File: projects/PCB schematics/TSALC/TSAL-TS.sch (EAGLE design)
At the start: 29 parts, among them J1 2P_1-770166-0, J2 2P_1-770166-0, J3 2P_1-770166-0, J4 2P_1-770166-0, X2 5566-2, X3 5566-2

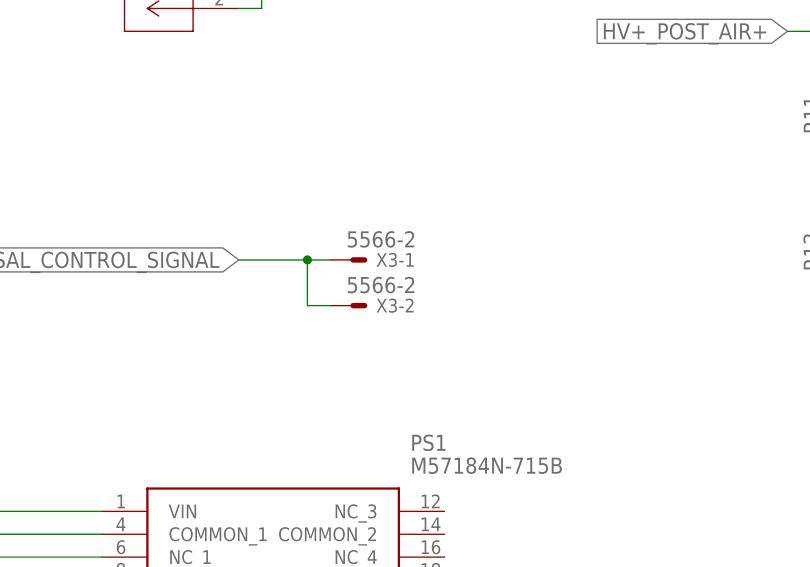
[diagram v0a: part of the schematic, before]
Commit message: TSALC - TS; Rev A.
Adding in silkscreen markings.
Board has TS and GLV markings separated by 8.26mm. This is the limit imposed by the optocoupler. The rules state that optocouplers are exempt. However, they will likely consider any copper leading up to the device to be TS components to be dealt with.

TSALC - TS; Rev A. Pull request #5.

TSALC boards now ready for pull request review.
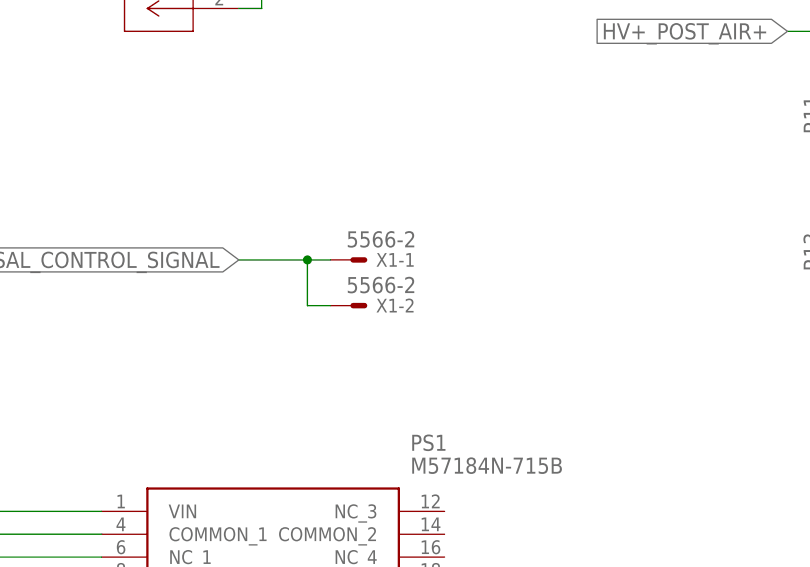
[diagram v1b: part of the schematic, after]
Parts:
- renumbered X3 to X1
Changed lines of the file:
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@@
 <part name="R2" library="rcl" library_urn="urn:adsk.eagle:library:334" deviceset="R-US_" device="R0805" package3d_urn="urn:adsk.eagle:package:23553/2" value="180"/>
 <part name="X2" library="con-molex" library_urn="urn:adsk.eagle:library:165" deviceset="5566-2" device="" package3d_urn="urn:adsk.eagle:package:8078583/1"/>
-<part name="X3" library="con-molex" library_urn="urn:adsk.eagle:library:165" deviceset="5566-2" device="" package3d_urn="urn:adsk.eagle:package:8078583/1"/>
+<part name="X1" library="con-molex" library_urn="urn:adsk.eagle:library:165" deviceset="5566-2" device="" package3d_urn="urn:adsk.eagle:package:8078583/1"/>
 <part name="PS1" library="M57184N-715B" deviceset="M57184N-715B" device=""/>
 <part name="L1" library="rcl" library_urn="urn:adsk.eagle:library:334" deviceset="L-US" device="L2012C" package3d_urn="urn:adsk.eagle:package:23475/2" value="1mH"/>
@@
 <attribute name="VALUE" x="22.098" y="75.057" size="1.778" layer="96"/>
 </instance>
-<instance part="X3" gate="-1" x="78.74" y="78.74" smashed="yes">
+<instance part="X1" gate="-1" x="78.74" y="78.74" smashed="yes">
 <attribute name="NAME" x="81.28" y="77.978" size="1.524" layer="95"/>
 <attribute name="VALUE" x="77.978" y="80.137" size="1.778" layer="96"/>
 </instance>
-<instance part="X3" gate="-2" x="78.74" y="73.66" smashed="yes">
+<instance part="X1" gate="-2" x="78.74" y="73.66" smashed="yes">
 <attribute name="NAME" x="81.28" y="72.898" size="1.524" layer="95"/>
 <attribute name="VALUE" x="77.978" y="75.057" size="1.778" layer="96"/>
@@
 <net name="TSAL_CONTROL_SIGNAL" class="0">
 <segment>
-<pinref part="X3" gate="-1" pin="S"/>
+<pinref part="X1" gate="-1" pin="S"/>
 <wire x1="76.2" y1="78.74" x2="73.66" y2="78.74" width="0.1524" layer="91"/>
 <wire x1="73.66" y1="78.74" x2="73.66" y2="73.66" width="0.1524" layer="91"/>
-<pinref part="X3" gate="-2" pin="S"/>
+<pinref part="X1" gate="-2" pin="S"/>
 <wire x1="73.66" y1="73.66" x2="76.2" y2="73.66" width="0.1524" layer="91"/>
 <wire x1="73.66" y1="78.74" x2="66.04" y2="78.74" width="0.1524" layer="91"/>

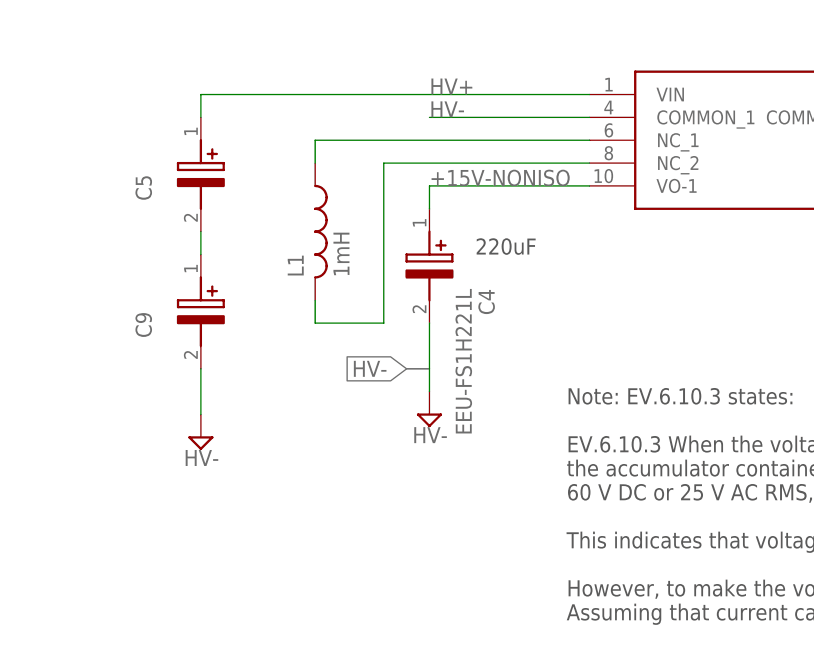
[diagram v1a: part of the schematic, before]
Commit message: TSALC - Capacitors updated with new EDA files.
Capacitors now current.
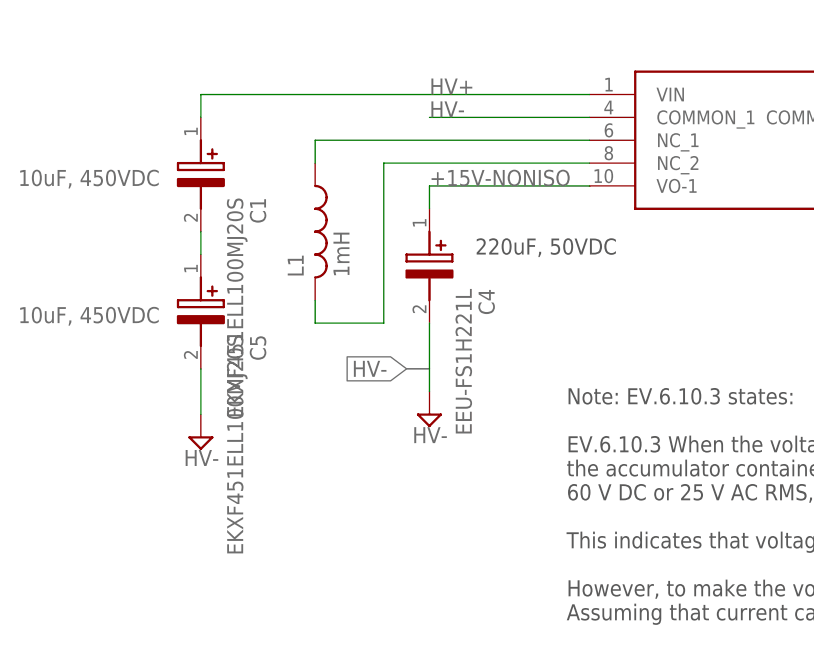
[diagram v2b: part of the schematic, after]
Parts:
- removed C9: EEU-FS1H221L, EEU-FS1H221L:EEU-FS1H221L
- added C1: EKXF451ELL100MJ20S, EKXF451ELL100MJ20S:EKXF451ELL100MJ20S
- C5: value EEU-FS1H221L -> EKXF451ELL100MJ20S; device EEU-FS1H221L:EEU-FS1H221L -> EKXF451ELL100MJ20S:EKXF451ELL100MJ20S
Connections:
- net HV+: now also C1.+; no longer C5.+
- net HV-: now also C5.-; no longer C9.-
- net N$3: now also C1.-, C5.+; no longer C5.-, C9.+
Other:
- note added: "10uF, 450VDC"
- note added: "220uF, 50VDC"
- note removed: "220uF"
- moved on the sheet: C5
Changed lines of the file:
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@@
 <part name="C4" library="EEU-FS1H221L" deviceset="EEU-FS1H221L" device=""/>
 <part name="SUPPLY8" library="supply2" library_urn="urn:adsk.eagle:library:372" deviceset="GND" device="" value="HV-"/>
-<part name="C5" library="EEU-FS1H221L" deviceset="EEU-FS1H221L" device=""/>
-<part name="C9" library="EEU-FS1H221L" deviceset="EEU-FS1H221L" device=""/>
 <part name="SUPPLY9" library="supply2" library_urn="urn:adsk.eagle:library:372" deviceset="GND" device="" value="HV-"/>
 <part name="C10" library="T491C106K020AT" deviceset="T491C106K020AT" device=""/>
@@
 <part name="R6" library="rcl" library_urn="urn:adsk.eagle:library:334" deviceset="R-US_" device="R0805" package3d_urn="urn:adsk.eagle:package:23553/2" value="10k"/>
 <part name="R7" library="rcl" library_urn="urn:adsk.eagle:library:334" deviceset="R-US_" device="R0805" package3d_urn="urn:adsk.eagle:package:23553/2" value="10k"/>
+<part name="C1" library="EKXF451ELL100MJ20S" deviceset="EKXF451ELL100MJ20S" device=""/>
+<part name="C5" library="EKXF451ELL100MJ20S" deviceset="EKXF451ELL100MJ20S" device=""/>
 </parts>
 <sheets>
@@
 <wire x1="218.44" y1="30.48" x2="220.98" y2="30.48" width="0.1524" layer="97"/>
 <wire x1="284.48" y1="71.12" x2="287.02" y2="71.12" width="0.1524" layer="97"/>
-<text x="38.1" y="33.02" size="1.778" layer="97">220uF</text>
+<text x="38.1" y="33.02" size="1.778" layer="97">220uF, 50VDC</text>
 <wire x1="30.48" y1="20.32" x2="33.02" y2="20.32" width="0.1524" layer="97"/>
 <wire x1="172.72" y1="53.34" x2="170.18" y2="53.34" width="0.1524" layer="255"/>
@@
 However, to make the voltage levels in the comparator work, HV- and post AIR- must be tied.
 Assuming that current cannot flow between these points, I've added 5x10k resistors to separate these out.</text>
+<text x="-12.7" y="40.64" size="1.778" layer="96">10uF, 450VDC</text>
+<text x="-12.7" y="25.4" size="1.778" layer="96">10uF, 450VDC</text>
 </plain>
 <instances>
@@
 <attribute name="VALUE" x="31.115" y="12.065" size="1.778" layer="96"/>
 </instance>
-<instance part="C5" gate="G$1" x="7.62" y="48.26" smashed="yes" rot="R270">
-<attribute name="NAME" x="1.27" y="41.91" size="1.778" layer="95" rot="R270" align="center-left"/>
-</instance>
-<instance part="C9" gate="G$1" x="7.62" y="33.02" smashed="yes" rot="R270">
-<attribute name="NAME" x="1.27" y="26.67" size="1.778" layer="95" rot="R270" align="center-left"/>
-</instance>
 <instance part="SUPPLY9" gate="GND" x="7.62" y="12.7" smashed="yes">
 <attribute name="VALUE" x="5.715" y="9.525" size="1.778" layer="96"/>
@@
 <attribute name="NAME" x="138.43" y="6.1214" size="1.778" layer="95" rot="R180"/>
 <attribute name="VALUE" x="138.43" y="10.922" size="1.778" layer="96" rot="R180"/>
+</instance>
+<instance part="C1" gate="G$1" x="7.62" y="48.26" smashed="yes" rot="R270">
+<attribute name="NAME" x="13.97" y="39.37" size="1.778" layer="95" rot="R270" align="center-left"/>
+<attribute name="VALUE" x="11.43" y="39.37" size="1.778" layer="96" rot="R270" align="center-left"/>
+</instance>
+<instance part="C5" gate="G$1" x="7.62" y="33.02" smashed="yes" rot="R270">
+<attribute name="NAME" x="13.97" y="24.13" size="1.778" layer="95" rot="R270" align="center-left"/>
+<attribute name="VALUE" x="11.43" y="24.13" size="1.778" layer="96" rot="R270" align="center-left"/>
 </instance>
 </instances>
@@
 <segment>
 <pinref part="SUPPLY9" gate="GND" pin="GND"/>
-<pinref part="C9" gate="G$1" pin="-"/>
 <wire x1="7.62" y1="15.24" x2="7.62" y2="20.32" width="0.1524" layer="91"/>
+<pinref part="C5" gate="G$1" pin="-"/>
 </segment>
 <segment>
@@
 <label x="33.02" y="50.8" size="1.778" layer="95"/>
 <wire x1="50.8" y1="50.8" x2="7.62" y2="50.8" width="0.1524" layer="91"/>
-<pinref part="C5" gate="G$1" pin="+"/>
 <wire x1="7.62" y1="50.8" x2="7.62" y2="48.26" width="0.1524" layer="91"/>
+<pinref part="C1" gate="G$1" pin="+"/>
 </segment>
 <segment>
@@
 <net name="N$3" class="0">
 <segment>
-<pinref part="C5" gate="G$1" pin="-"/>
-<pinref part="C9" gate="G$1" pin="+"/>
 <wire x1="7.62" y1="35.56" x2="7.62" y2="33.02" width="0.1524" layer="91"/>
-</segment>
-</net>
+<pinref part="C1" gate="G$1" pin="-"/>
+<pinref part="C5" gate="G$1" pin="+"/>
+</segment>
+</net>

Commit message: TSAL - Minor fixes.
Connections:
- net HV+_POST_AIR+ renamed MOTORCONTROLLER+
- net HV-_POST_AIR- renamed MOTORCONTROLLER-
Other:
- moved on the sheet: J3, J4
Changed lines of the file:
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@@
 <attribute name="NAME" x="11.0744" y="129.7686" size="2.0828" layer="95" ratio="6" rot="SMR0"/>
 </instance>
-<instance part="J3" gate="A" x="66.04" y="124.46" smashed="yes" rot="MR0">
-<attribute name="NAME" x="61.8744" y="129.7686" size="2.0828" layer="95" ratio="6" rot="SMR0"/>
-</instance>
-<instance part="J4" gate="A" x="66.04" y="109.22" smashed="yes" rot="MR0">
-<attribute name="NAME" x="61.8744" y="114.5286" size="2.0828" layer="95" ratio="6" rot="SMR0"/>
+<instance part="J3" gate="A" x="71.12" y="124.46" smashed="yes" rot="MR0">
+<attribute name="NAME" x="66.9544" y="129.7686" size="2.0828" layer="95" ratio="6" rot="SMR0"/>
+</instance>
+<instance part="J4" gate="A" x="71.12" y="109.22" smashed="yes" rot="MR0">
+<attribute name="NAME" x="66.9544" y="114.5286" size="2.0828" layer="95" ratio="6" rot="SMR0"/>
 </instance>
 <instance part="R3" gate="G$1" x="121.92" y="15.24" smashed="yes">
@@
 </segment>
 <segment>
-<wire x1="66.04" y1="109.22" x2="68.58" y2="109.22" width="0.1524" layer="91"/>
-<wire x1="68.58" y1="109.22" x2="68.58" y2="106.68" width="0.1524" layer="91"/>
-<wire x1="68.58" y1="106.68" x2="66.04" y2="106.68" width="0.1524" layer="91"/>
-<wire x1="68.58" y1="109.22" x2="73.66" y2="109.22" width="0.1524" layer="91"/>
-<junction x="68.58" y="109.22"/>
-<label x="73.66" y="109.22" size="1.778" layer="95" xref="yes"/>
+<wire x1="71.12" y1="109.22" x2="73.66" y2="109.22" width="0.1524" layer="91"/>
+<wire x1="73.66" y1="109.22" x2="73.66" y2="106.68" width="0.1524" layer="91"/>
+<wire x1="73.66" y1="106.68" x2="71.12" y2="106.68" width="0.1524" layer="91"/>
+<wire x1="73.66" y1="109.22" x2="78.74" y2="109.22" width="0.1524" layer="91"/>
+<junction x="73.66" y="109.22"/>
+<label x="78.74" y="109.22" size="1.778" layer="95" xref="yes"/>
 <pinref part="J4" gate="A" pin="1"/>
 <pinref part="J4" gate="A" pin="2"/>
@@
 <pinref part="HV-OPA" gate="G$1" pin="OUT"/>
 <wire x1="193.04" y1="38.1" x2="177.8" y2="38.1" width="0.1524" layer="91"/>
-</segment>
-</net>
-<net name="HV+_POST_AIR+" class="0">
-<segment>
-<wire x1="15.24" y1="124.46" x2="17.78" y2="124.46" width="0.1524" layer="91"/>
-<wire x1="17.78" y1="124.46" x2="17.78" y2="121.92" width="0.1524" layer="91"/>
-<wire x1="17.78" y1="121.92" x2="15.24" y2="121.92" width="0.1524" layer="91"/>
-<wire x1="17.78" y1="124.46" x2="22.86" y2="124.46" width="0.1524" layer="91"/>
-<junction x="17.78" y="124.46"/>
-<label x="22.86" y="124.46" size="1.778" layer="95" xref="yes"/>
-<pinref part="J2" gate="A" pin="1"/>
-<pinref part="J2" gate="A" pin="2"/>
-</segment>
-<segment>
-<wire x1="127" y1="104.14" x2="132.08" y2="104.14" width="0.1524" layer="91"/>
-<wire x1="132.08" y1="104.14" x2="132.08" y2="101.6" width="0.1524" layer="91"/>
-<pinref part="R11" gate="G$1" pin="2"/>
-<label x="127" y="104.14" size="1.778" layer="95" rot="R180" xref="yes"/>
 </segment>
 </net>
@@
 </segment>
 </net>
-<net name="HV-_POST_AIR-" class="0">
-<segment>
-<wire x1="66.04" y1="124.46" x2="68.58" y2="124.46" width="0.1524" layer="91"/>
-<wire x1="68.58" y1="124.46" x2="68.58" y2="121.92" width="0.1524" layer="91"/>
-<wire x1="68.58" y1="121.92" x2="66.04" y2="121.92" width="0.1524" layer="91"/>
-<wire x1="68.58" y1="124.46" x2="73.66" y2="124.46" width="0.1524" layer="91"/>
-<junction x="68.58" y="124.46"/>
-<label x="73.66" y="124.46" size="1.778" layer="95" xref="yes"/>
+<net name="N$5" class="0">
+<segment>
+<pinref part="R3" gate="G$1" pin="2"/>
+<pinref part="R4" gate="G$1" pin="1"/>
+<wire x1="127" y1="15.24" x2="129.54" y2="15.24" width="0.1524" layer="91"/>
+</segment>
+</net>
+<net name="N$6" class="0">
+<segment>
+<pinref part="R4" gate="G$1" pin="2"/>
+<pinref part="R5" gate="G$1" pin="1"/>
+<wire x1="139.7" y1="15.24" x2="142.24" y2="15.24" width="0.1524" layer="91"/>
+</segment>
+</net>
+<net name="N$7" class="0">
+<segment>
+<pinref part="R5" gate="G$1" pin="2"/>
+<wire x1="152.4" y1="15.24" x2="154.94" y2="15.24" width="0.1524" layer="91"/>
+<wire x1="154.94" y1="15.24" x2="154.94" y2="7.62" width="0.1524" layer="91"/>
+<pinref part="R6" gate="G$1" pin="1"/>
+<wire x1="154.94" y1="7.62" x2="152.4" y2="7.62" width="0.1524" layer="91"/>
+</segment>
+</net>
+<net name="N$8" class="0">
+<segment>
+<pinref part="R6" gate="G$1" pin="2"/>
+<pinref part="R7" gate="G$1" pin="1"/>
+<wire x1="142.24" y1="7.62" x2="139.7" y2="7.62" width="0.1524" layer="91"/>
+</segment>
+</net>
+<net name="THERMAL" class="0">
+<segment>
+<pinref part="HV-OPA" gate="G$1" pin="E/DCOM1"/>
+<wire x1="167.64" y1="27.94" x2="167.64" y2="20.32" width="0.1524" layer="91"/>
+<wire x1="167.64" y1="20.32" x2="182.88" y2="20.32" width="0.1524" layer="91"/>
+<label x="170.18" y="20.32" size="1.778" layer="95"/>
+</segment>
+</net>
+<net name="MOTORCONTROLLER+" class="0">
+<segment>
+<wire x1="15.24" y1="124.46" x2="17.78" y2="124.46" width="0.1524" layer="91"/>
+<wire x1="17.78" y1="124.46" x2="17.78" y2="121.92" width="0.1524" layer="91"/>
+<wire x1="17.78" y1="121.92" x2="15.24" y2="121.92" width="0.1524" layer="91"/>
+<wire x1="17.78" y1="124.46" x2="22.86" y2="124.46" width="0.1524" layer="91"/>
+<junction x="17.78" y="124.46"/>
+<label x="22.86" y="124.46" size="1.778" layer="95" xref="yes"/>
+<pinref part="J2" gate="A" pin="1"/>
+<pinref part="J2" gate="A" pin="2"/>
+</segment>
+<segment>
+<wire x1="127" y1="104.14" x2="132.08" y2="104.14" width="0.1524" layer="91"/>
+<wire x1="132.08" y1="104.14" x2="132.08" y2="101.6" width="0.1524" layer="91"/>
+<pinref part="R11" gate="G$1" pin="2"/>
+<label x="127" y="104.14" size="1.778" layer="95" rot="R180" xref="yes"/>
+</segment>
+</net>
+<net name="MOTORCONTROLLER-" class="0">
+<segment>
+<wire x1="71.12" y1="124.46" x2="73.66" y2="124.46" width="0.1524" layer="91"/>
+<wire x1="73.66" y1="124.46" x2="73.66" y2="121.92" width="0.1524" layer="91"/>
+<wire x1="73.66" y1="121.92" x2="71.12" y2="121.92" width="0.1524" layer="91"/>
+<wire x1="73.66" y1="124.46" x2="78.74" y2="124.46" width="0.1524" layer="91"/>
+<junction x="73.66" y="124.46"/>
+<label x="78.74" y="124.46" size="1.778" layer="95" xref="yes"/>
 <pinref part="J3" gate="A" pin="1"/>
 <pinref part="J3" gate="A" pin="2"/>
@@
 <wire x1="116.84" y1="15.24" x2="114.3" y2="15.24" width="0.1524" layer="91"/>
 <wire x1="114.3" y1="15.24" x2="114.3" y2="27.94" width="0.1524" layer="91"/>
-<wire x1="114.3" y1="27.94" x2="96.52" y2="27.94" width="0.1524" layer="91"/>
-<label x="96.52" y="27.94" size="1.778" layer="95"/>
-</segment>
-</net>
-<net name="N$5" class="0">
-<segment>
-<pinref part="R3" gate="G$1" pin="2"/>
-<pinref part="R4" gate="G$1" pin="1"/>
-<wire x1="127" y1="15.24" x2="129.54" y2="15.24" width="0.1524" layer="91"/>
-</segment>
-</net>
-<net name="N$6" class="0">
-<segment>
-<pinref part="R4" gate="G$1" pin="2"/>
-<pinref part="R5" gate="G$1" pin="1"/>
-<wire x1="139.7" y1="15.24" x2="142.24" y2="15.24" width="0.1524" layer="91"/>
-</segment>
-</net>
-<net name="N$7" class="0">
-<segment>
-<pinref part="R5" gate="G$1" pin="2"/>
-<wire x1="152.4" y1="15.24" x2="154.94" y2="15.24" width="0.1524" layer="91"/>
-<wire x1="154.94" y1="15.24" x2="154.94" y2="7.62" width="0.1524" layer="91"/>
-<pinref part="R6" gate="G$1" pin="1"/>
-<wire x1="154.94" y1="7.62" x2="152.4" y2="7.62" width="0.1524" layer="91"/>
-</segment>
-</net>
-<net name="N$8" class="0">
-<segment>
-<pinref part="R6" gate="G$1" pin="2"/>
-<pinref part="R7" gate="G$1" pin="1"/>
-<wire x1="142.24" y1="7.62" x2="139.7" y2="7.62" width="0.1524" layer="91"/>
-</segment>
-</net>
-<net name="THERMAL" class="0">
-<segment>
-<pinref part="HV-OPA" gate="G$1" pin="E/DCOM1"/>
-<wire x1="167.64" y1="27.94" x2="167.64" y2="20.32" width="0.1524" layer="91"/>
-<wire x1="167.64" y1="20.32" x2="182.88" y2="20.32" width="0.1524" layer="91"/>
-<label x="170.18" y="20.32" size="1.778" layer="95"/>
-</segment>
-</net>
+<wire x1="114.3" y1="27.94" x2="86.36" y2="27.94" width="0.1524" layer="91"/>
+<label x="86.36" y="27.94" size="1.778" layer="95"/>
+</segment>
+</net>

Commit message: TSAL - Added in FUSE to HV sense line.
Added in FUSE and removed redundant tantalum capacitors.
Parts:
- removed C10, C11: T491C106K020AT, T491C106K020AT:T491C106K020AT
- added F1: 0885001.DR, 0885001.DR:0885001.DR
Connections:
- new net MOTORCONTROLLER+_POST_FUSE: F1.2, R11.2
- net +15V-NONISO: no longer C11.1
- net +8V: no longer C10.1
- net HV-: no longer C10.2, C11.2
- net MOTORCONTROLLER+: now also F1.1; no longer R11.2
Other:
- moved on the sheet: J1, J2, J3, J4
